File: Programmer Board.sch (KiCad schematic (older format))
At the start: 9 parts, among them J1 105-1103-001, J10 Conn_01x03, J11 105-1102-001, J12 105-1103-001, J2 Conn_01x03, J3 105-1102-001, J8 Conn_01x02, J9 Conn_02x18_Odd_Even

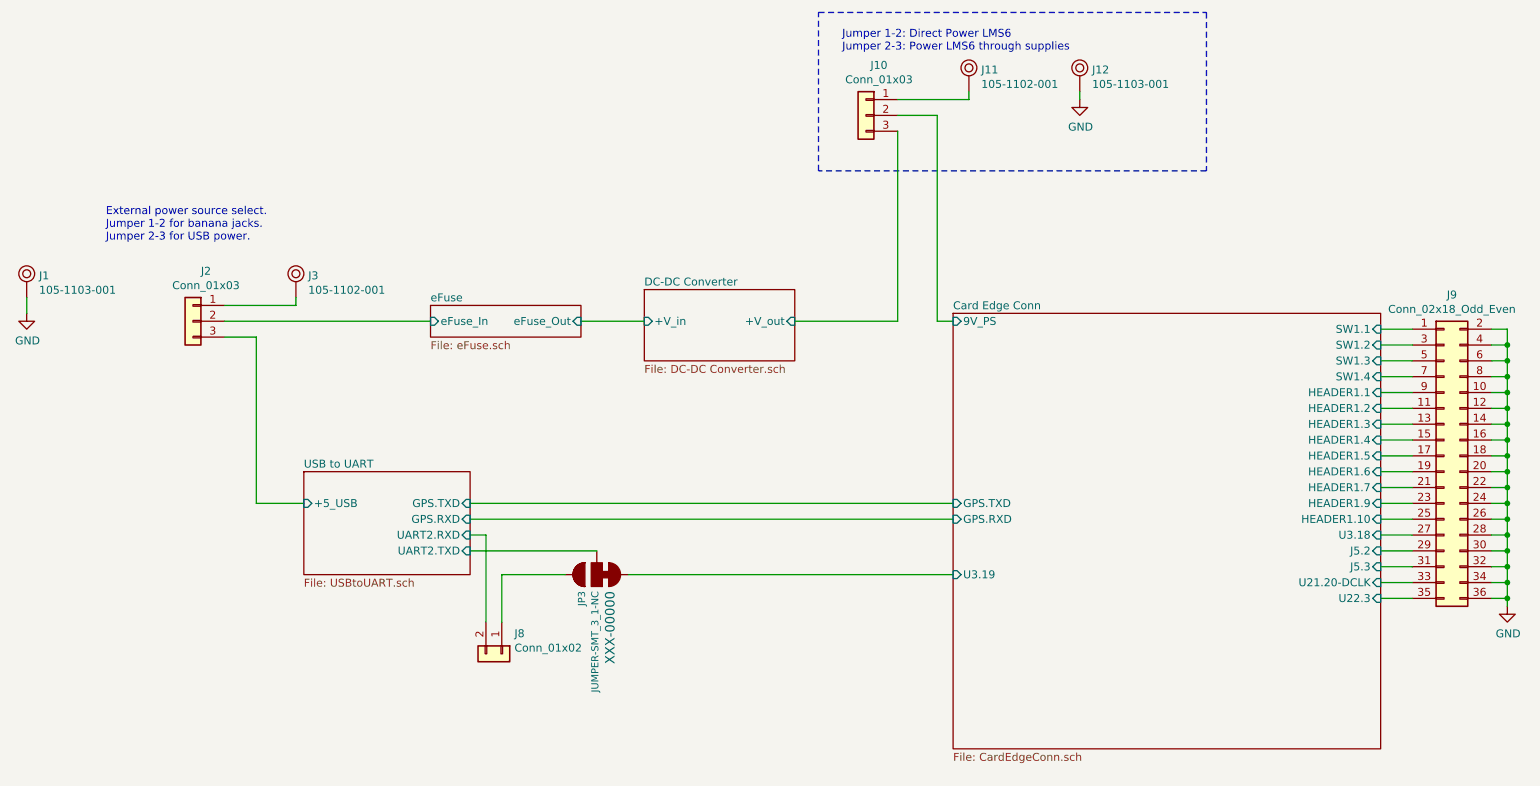
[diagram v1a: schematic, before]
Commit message: Changed J9 connections to help with layout.
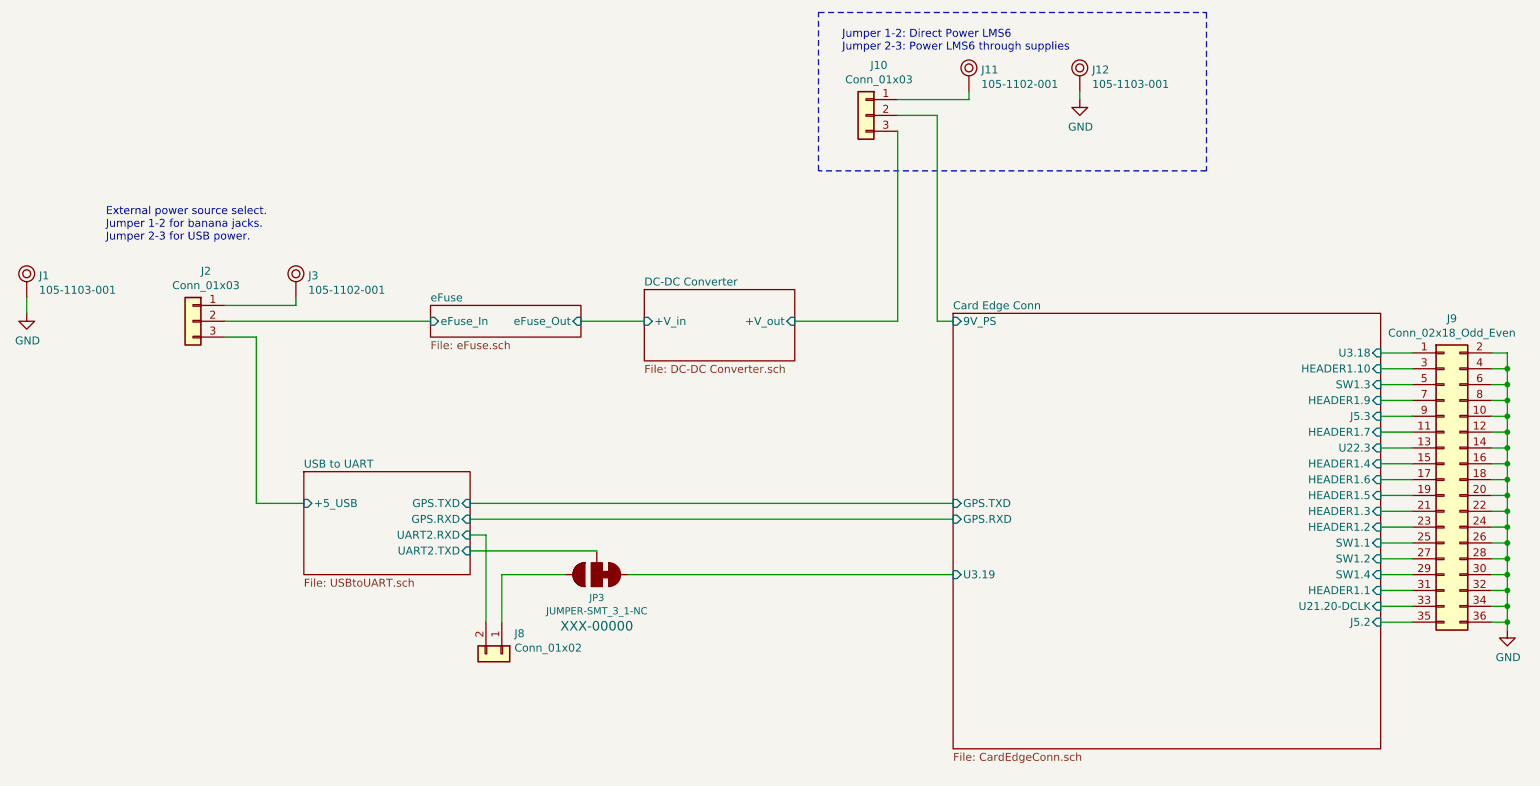
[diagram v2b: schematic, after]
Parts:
- JP3: footprint SMT-JUMPER_3_1-NC -> Jumpers:SMT-JUMPER_3_1-NC_TRACE_NO-SILK
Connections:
- net Card Edge Conn/HEADER1.1: now also J9.31 (Pin_31); no longer J9.9 (Pin_9)
- net Card Edge Conn/HEADER1.10: now also J9.3 (Pin_3); no longer J9.25 (Pin_25)
- net Card Edge Conn/HEADER1.2: now also J9.23 (Pin_23); no longer J9.11 (Pin_11)
- net Card Edge Conn/HEADER1.3: now also J9.21 (Pin_21); no longer J9.13 (Pin_13)
- net Card Edge Conn/HEADER1.5: now also J9.19 (Pin_19); no longer J9.17 (Pin_17)
- net Card Edge Conn/HEADER1.6: now also J9.17 (Pin_17); no longer J9.19 (Pin_19)
- net Card Edge Conn/HEADER1.7: now also J9.11 (Pin_11); no longer J9.21 (Pin_21)
- net Card Edge Conn/HEADER1.9: now also J9.7 (Pin_7); no longer J9.23 (Pin_23)
- net Card Edge Conn/J5.2: now also J9.35 (Pin_35); no longer J9.29 (Pin_29)
- net Card Edge Conn/J5.3: now also J9.9 (Pin_9); no longer J9.31 (Pin_31)
- net Card Edge Conn/SW1.1: now also J9.25 (Pin_25); no longer J9.1 (Pin_1)
- net Card Edge Conn/SW1.2: now also J9.27 (Pin_27); no longer J9.3 (Pin_3)
- net Card Edge Conn/SW1.4: now also J9.29 (Pin_29); no longer J9.7 (Pin_7)
- net Card Edge Conn/U22.3: now also J9.13 (Pin_13); no longer J9.35 (Pin_35)
- net Card Edge Conn/U3.18: now also J9.1 (Pin_1); no longer J9.27 (Pin_27)
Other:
- moved on the sheet: J9
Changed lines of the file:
@@
 Title "LMS6 Interface Board"
 Date "2020-10-17"
-Rev "5"
+Rev "6"
 Comp ""
-Comment1 "Rev 2: Added eFuse. Power Configurations."
-Comment2 "Rev 3: Changed sheet to US Letter"
-Comment3 "Rev 4: Fixed J9 hanging over border of sheet."
-Comment4 "Rev 5: Fixed J6 footprint and MPN info."
+Comment1 "Rev 3: Changed sheet to US Letter"
+Comment2 "Rev 4: Fixed J9 hanging over border of sheet."
+Comment3 "Rev 5: Fixed J6 footprint and MPN info."
+Comment4 "Rev 6: Fixed footprint issues. Changed J9 connections for layout."
 $EndDescr
 $Sheet
@@
 F0 "Card Edge Conn" 50
 F1 "CardEdgeConn.sch" 50
-F2 "U21.20-DCLK" I R 9450 4950 50
-F3 "SW1.1" I R 9450 3350 50
+F2 "U21.20-DCLK" I R 9450 5100 50
+F3 "SW1.1" I R 9450 4700 50
 F4 "GPS.TXD" I L 6750 4450 50
-F5 "U22.3" I R 9450 5050 50
-F6 "J5.3" I R 9450 4850 50
-F7 "SW1.3" I R 9450 3550 50
-F8 "U3.18" I R 9450 4650 50
+F5 "U22.3" I R 9450 4100 50
+F6 "J5.3" I R 9450 3900 50
+F7 "SW1.3" I R 9450 3700 50
+F8 "U3.18" I R 9450 3500 50
 F9 "GPS.RXD" I L 6750 4550 50
 F10 "U3.19" I L 6750 4900 50
-F11 "SW1.2" I R 9450 3450 50
-F12 "SW1.4" I R 9450 3650 50
-F13 "J5.2" I R 9450 4750 50
-F14 "HEADER1.1" I R 9450 3750 50
-F15 "HEADER1.2" I R 9450 3850 50
-F16 "HEADER1.3" I R 9450 3950 50
-F17 "HEADER1.4" I R 9450 4050 50
-F18 "HEADER1.5" I R 9450 4150 50
-F19 "HEADER1.6" I R 9450 4250 50
-F20 "HEADER1.7" I R 9450 4350 50
-F21 "HEADER1.9" I R 9450 4450 50
-F22 "HEADER1.10" I R 9450 4550 50
+F11 "SW1.2" I R 9450 4800 50
+F12 "SW1.4" I R 9450 4900 50
+F13 "J5.2" I R 9450 5200 50
+F14 "HEADER1.1" I R 9450 5000 50
+F15 "HEADER1.2" I R 9450 4600 50
+F16 "HEADER1.3" I R 9450 4500 50
+F17 "HEADER1.4" I R 9450 4200 50
+F18 "HEADER1.5" I R 9450 4400 50
+F19 "HEADER1.6" I R 9450 4300 50
+F20 "HEADER1.7" I R 9450 4000 50
+F21 "HEADER1.9" I R 9450 3800 50
+F22 "HEADER1.10" I R 9450 3600 50
 F23 "9V_PS" I L 6750 3300 50
 $EndSheet
@@
 AR Path="/5F7C6408/5F8F06E0" Ref="JP?"  Part="1"
 AR Path="/5F8F06E0" Ref="JP3"  Part="1"
-F 0 "JP3" H 4604 4995 45  0000 L CNN
-F 1 "JUMPER-SMT_3_1-NC" H 4604 4911 45  0000 L CNN
-F 2 "SMT-JUMPER_3_1-NC" H 4500 5150 20  0001 C CNN
+F 0 "JP3" V 4646 4900 45  0000 C CNN
+F 1 "JUMPER-SMT_3_1-NC" V 4730 4900 45  0000 C CNN
+F 2 "Jumpers:SMT-JUMPER_3_1-NC_TRACE_NO-SILK" H 4500 5150 20  0001 C CNN
 F 3 "" V 4500 4845 60  0001 C CNN
-F 4 "XXX-00000" H 4604 4816 60  0000 L CNN "PROD_ID"
+F 4 "XXX-00000" V 4825 4900 60  0000 C CNN "PROD_ID"
 	1    4500 4900
 	0    -1   1    0
@@
 L Connector_Generic:Conn_02x18_Odd_Even J9
 U 1 1 5F8F3B51
-P 9850 4150
-F 0 "J9" H 9900 5167 50  0000 C CNN
-F 1 "Conn_02x18_Odd_Even" H 9900 5076 50  0000 C CNN
-F 2 "Connector_PinHeader_2.54mm:PinHeader_2x18_P2.54mm_Vertical" H 9850 4150 50  0001 C CNN
-F 3 "https://drawings-pdf.s3.amazonaws.com/11636.pdf" H 9850 4150 50  0001 C CNN
-F 4 "Sullins Connector Solutions" H 9850 4150 50  0001 C CNN "Manufacturer"
-F 5 "PREC020DAAN-RC" H 9850 4150 50  0001 C CNN "MPN"
-	1    9850 4150
-	1    0    0    -1
-$EndComp
-Wire Wire Line
-	9650 3350 9450 3350
-Wire Wire Line
-	9450 3450 9650 3450
-Wire Wire Line
-	9650 3550 9450 3550
-Wire Wire Line
-	9450 3650 9650 3650
-Wire Wire Line
-	9650 3750 9450 3750
-Wire Wire Line
-	9450 3850 9650 3850
-Wire Wire Line
-	9650 3950 9450 3950
-Wire Wire Line
-	9450 4050 9650 4050
-Wire Wire Line
-	9650 4150 9450 4150
-Wire Wire Line
-	9450 4250 9650 4250
-Wire Wire Line
-	9650 4350 9450 4350
-Wire Wire Line
-	9450 4450 9650 4450
-Wire Wire Line
-	9650 4550 9450 4550
-Wire Wire Line
-	9450 4650 9650 4650
-Wire Wire Line
-	9650 4750 9450 4750
-Wire Wire Line
-	9450 4850 9650 4850
-Wire Wire Line
-	9650 4950 9450 4950
-Wire Wire Line
-	9450 5050 9650 5050
+P 9850 4300
+F 0 "J9" H 9900 5317 50  0000 C CNN
+F 1 "Conn_02x18_Odd_Even" H 9900 5226 50  0000 C CNN
+F 2 "Connector_PinHeader_2.54mm:PinHeader_2x18_P2.54mm_Vertical" H 9850 4300 50  0001 C CNN
+F 3 "https://drawings-pdf.s3.amazonaws.com/11636.pdf" H 9850 4300 50  0001 C CNN
+F 4 "Sullins Connector Solutions" H 9850 4300 50  0001 C CNN "Manufacturer"
+F 5 "PREC020DAAN-RC" H 9850 4300 50  0001 C CNN "MPN"
+	1    9850 4300
+	1    0    0    -1
+$EndComp
 $Comp
 L power:GND #PWR018
 U 1 1 5F8FB83E
-P 10250 5100
-F 0 "#PWR018" H 10250 4850 50  0001 C CNN
-F 1 "GND" H 10255 4927 50  0000 C CNN
-F 2 "" H 10250 5100 50  0001 C CNN
-F 3 "" H 10250 5100 50  0001 C CNN
-	1    10250 5100
-	1    0    0    -1
-$EndComp
-Wire Wire Line
-	10250 5100 10250 5050
-Wire Wire Line
-	10250 5050 10150 5050
-Wire Wire Line
-	10150 3350 10250 3350
-Connection ~ 10250 5050
-Wire Wire Line
-	10150 4950 10250 4950
-Connection ~ 10250 4950
-Wire Wire Line
-	10250 4950 10250 5050
-Wire Wire Line
-	10150 4850 10250 4850
-Connection ~ 10250 4850
-Wire Wire Line
-	10250 4850 10250 4950
-Wire Wire Line
-	10150 4750 10250 4750
-Connection ~ 10250 4750
-Wire Wire Line
-	10250 4750 10250 4850
-Wire Wire Line
-	10150 4650 10250 4650
-Connection ~ 10250 4650
-Wire Wire Line
-	10250 4650 10250 4750
-Wire Wire Line
-	10150 4550 10250 4550
-Connection ~ 10250 4550
-Wire Wire Line
-	10250 4550 10250 4650
-Wire Wire Line
-	10150 4450 10250 4450
-Connection ~ 10250 4450
-Wire Wire Line
-	10250 4450 10250 4550
-Wire Wire Line
-	10150 4350 10250 4350
-Connection ~ 10250 4350
-Wire Wire Line
-	10250 4350 10250 4450
-Wire Wire Line
-	10150 4250 10250 4250
-Wire Wire Line
-	10250 3350 10250 3450
-Connection ~ 10250 4250
-Wire Wire Line
-	10250 4250 10250 4350
-Wire Wire Line
-	10150 4150 10250 4150
-Connection ~ 10250 4150
-Wire Wire Line
-	10250 4150 10250 4250
-Wire Wire Line
-	10150 4050 10250 4050
-Connection ~ 10250 4050
-Wire Wire Line
-	10250 4050 10250 4150
-Wire Wire Line
-	10150 3950 10250 3950
-Connection ~ 10250 3950
-Wire Wire Line
-	10250 3950 10250 4050
-Wire Wire Line
-	10150 3850 10250 3850
-Connection ~ 10250 3850
-Wire Wire Line
-	10250 3850 10250 3950
-Wire Wire Line
-	10150 3750 10250 3750
-Connection ~ 10250 3750
-Wire Wire Line
-	10250 3750 10250 3850
-Wire Wire Line
-	10150 3650 10250 3650
-Connection ~ 10250 3650
-Wire Wire Line
-	10250 3650 10250 3750
-Wire Wire Line
-	10150 3550 10250 3550
-Connection ~ 10250 3550
-Wire Wire Line
-	10250 3550 10250 3650
-Wire Wire Line
-	10150 3450 10250 3450
-Connection ~ 10250 3450
-Wire Wire Line
-	10250 3450 10250 3550
+P 10250 5250
+F 0 "#PWR018" H 10250 5000 50  0001 C CNN
+F 1 "GND" H 10255 5077 50  0000 C CNN
+F 2 "" H 10250 5250 50  0001 C CNN
+F 3 "" H 10250 5250 50  0001 C CNN
+	1    10250 5250
+	1    0    0    -1
+$EndComp
+Wire Wire Line
+	10250 5250 10250 5200
+Wire Wire Line
+	10250 5200 10150 5200
+Wire Wire Line
+	10150 3500 10250 3500
+Connection ~ 10250 5200
+Wire Wire Line
+	10150 5100 10250 5100
+Connection ~ 10250 5100
+Wire Wire Line
+	10250 5100 10250 5200
+Wire Wire Line
+	10150 5000 10250 5000
+Connection ~ 10250 5000
+Wire Wire Line
+	10250 5000 10250 5100
+Wire Wire Line
+	10150 4900 10250 4900
+Connection ~ 10250 4900
+Wire Wire Line
+	10250 4900 10250 5000
+Wire Wire Line
+	10150 4800 10250 4800
+Connection ~ 10250 4800
+Wire Wire Line
+	10250 4800 10250 4900
+Wire Wire Line
+	10150 4700 10250 4700
+Connection ~ 10250 4700
+Wire Wire Line
+	10250 4700 10250 4800
+Wire Wire Line
+	10150 4600 10250 4600
+Connection ~ 10250 4600
+Wire Wire Line
+	10250 4600 10250 4700
+Wire Wire Line
+	10150 4500 10250 4500
+Connection ~ 10250 4500
+Wire Wire Line
+	10250 4500 10250 4600
+Wire Wire Line
+	10150 4400 10250 4400
+Wire Wire Line
+	10250 3500 10250 3600
+Connection ~ 10250 4400
+Wire Wire Line
+	10250 4400 10250 4500
+Wire Wire Line
+	10150 4300 10250 4300
+Connection ~ 10250 4300
+Wire Wire Line
+	10250 4300 10250 4400
+Wire Wire Line
+	10150 4200 10250 4200
+Connection ~ 10250 4200
+Wire Wire Line
+	10250 4200 10250 4300
+Wire Wire Line
+	10150 4100 10250 4100
+Connection ~ 10250 4100
+Wire Wire Line
+	10250 4100 10250 4200
+Wire Wire Line
+	10150 4000 10250 4000
+Connection ~ 10250 4000
+Wire Wire Line
+	10250 4000 10250 4100
+Wire Wire Line
+	10150 3900 10250 3900
+Connection ~ 10250 3900
+Wire Wire Line
+	10250 3900 10250 4000
+Wire Wire Line
+	10150 3800 10250 3800
+Connection ~ 10250 3800
+Wire Wire Line
+	10250 3800 10250 3900
+Wire Wire Line
+	10150 3700 10250 3700
+Connection ~ 10250 3700
+Wire Wire Line
+	10250 3700 10250 3800
+Wire Wire Line
+	10150 3600 10250 3600
+Connection ~ 10250 3600
+Wire Wire Line
+	10250 3600 10250 3700
 $Sheet
 S 3450 3200 950  200
@@
 Wire Notes Line
 	5900 2350 5900 1350
+Wire Wire Line
+	9450 3500 9650 3500
+Wire Wire Line
+	9450 3600 9650 3600
+Wire Wire Line
+	9450 3700 9650 3700
+Wire Wire Line
+	9450 3800 9650 3800
+Wire Wire Line
+	9450 3900 9650 3900
+Wire Wire Line
+	9450 4000 9650 4000
+Wire Wire Line
+	9450 4100 9650 4100
+Wire Wire Line
+	9450 4200 9650 4200
+Wire Wire Line
+	9450 4300 9650 4300
+Wire Wire Line
+	9450 4400 9650 4400
+Wire Wire Line
+	9450 4500 9650 4500
+Wire Wire Line
+	9450 4600 9650 4600
+Wire Wire Line
+	9450 4700 9650 4700
+Wire Wire Line
+	9450 4800 9650 4800
+Wire Wire Line
+	9450 4900 9650 4900
+Wire Wire Line
+	9450 5000 9650 5000
+Wire Wire Line
+	9450 5100 9650 5100
+Wire Wire Line
+	9450 5200 9650 5200
 $EndSCHEMATC

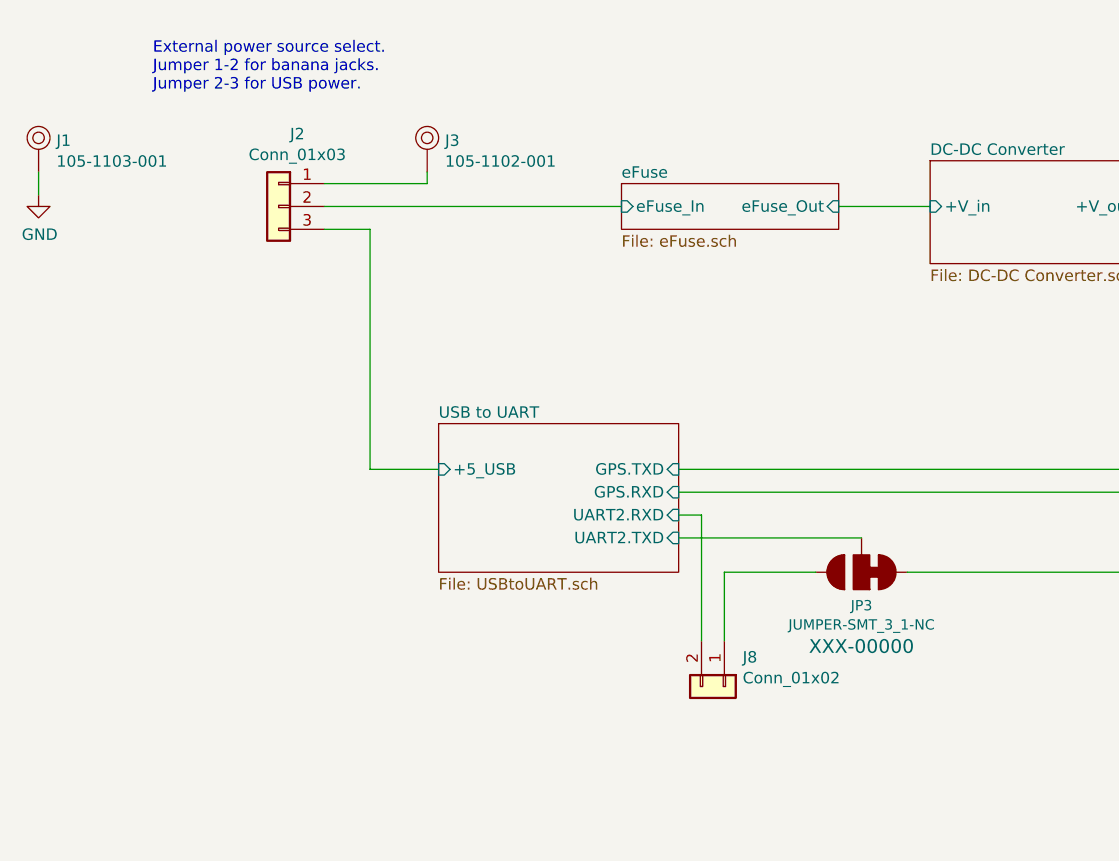
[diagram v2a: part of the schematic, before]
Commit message: Changed crystal for resonator. Board Layout.
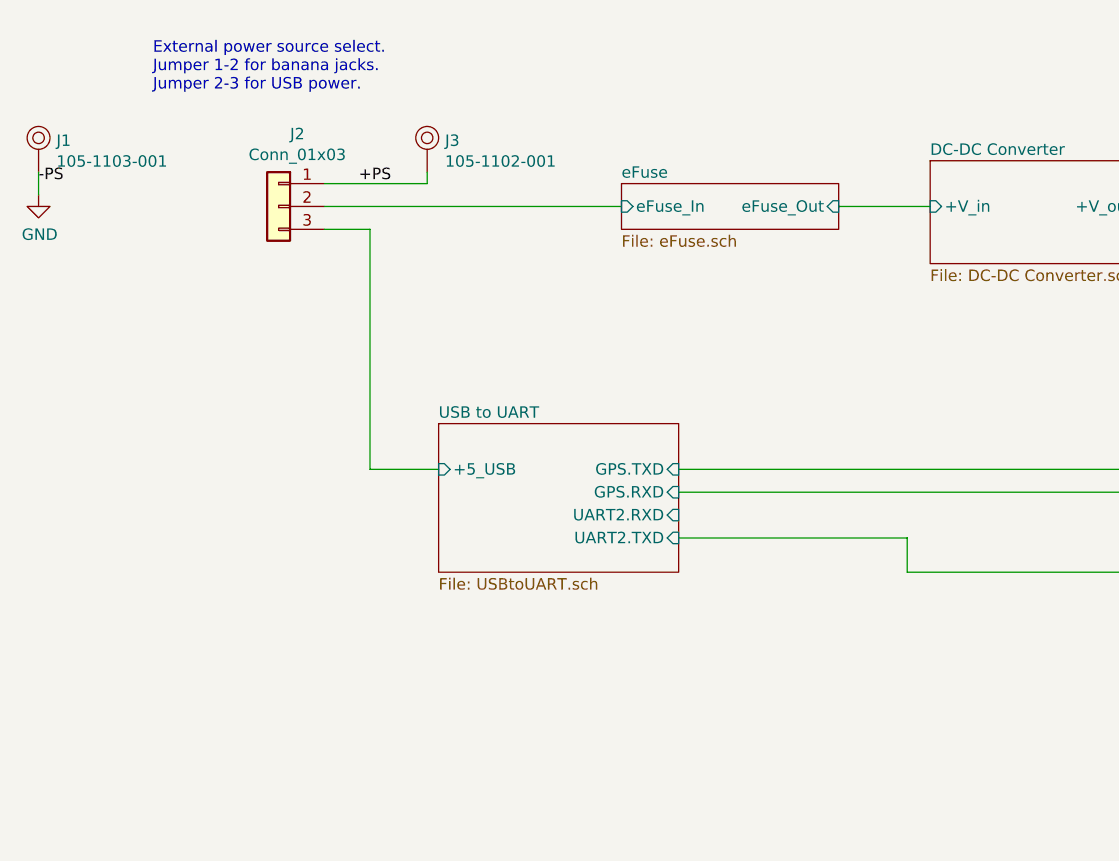
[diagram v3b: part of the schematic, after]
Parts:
- removed J8: Conn_01x02, Connector_PinHeader_2.54mm:PinHeader_1x02_P2.54mm_Vertical, symbol Connector_Generic:Conn_01x02
- removed JP3: JUMPER-SMT_3_1-NC, Jumpers:SMT-JUMPER_3_1-NC_TRACE_NO-SILK, symbol SparkFun-Jumpers:JUMPER-SMT_3_1-NC
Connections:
- net +PS: now reaches J2.1 (Pin_1), J3.1
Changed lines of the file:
@@
 Comment2 "Rev 4: Fixed J9 hanging over border of sheet."
 Comment3 "Rev 5: Fixed J6 footprint and MPN info."
-Comment4 "Rev 6: Fixed footprint issues. Changed J9 connections for layout."
+Comment4 "Rev 6: Fixed footprint issues. Changed J9 connections for layout. Changed Y1."
 $EndDescr
 $Sheet
@@
 Wire Wire Line
 	3700 4550 6750 4550
-$Comp
-L SparkFun-Jumpers:JUMPER-SMT_3_1-NC JP?
-U 1 1 5F8F06E0
-P 4500 4900
-AR Path="/5F7C6408/5F8F06E0" Ref="JP?"  Part="1"
-AR Path="/5F8F06E0" Ref="JP3"  Part="1"
-F 0 "JP3" V 4646 4900 45  0000 C CNN
-F 1 "JUMPER-SMT_3_1-NC" V 4730 4900 45  0000 C CNN
-F 2 "Jumpers:SMT-JUMPER_3_1-NC_TRACE_NO-SILK" H 4500 5150 20  0001 C CNN
-F 3 "" V 4500 4845 60  0001 C CNN
-F 4 "XXX-00000" V 4825 4900 60  0000 C CNN "PROD_ID"
-	1    4500 4900
-	0    -1   1    0
-$EndComp
-Wire Wire Line
-	3700 4750 4500 4750
 Wire Wire Line
 	4700 4900 6750 4900
-$Comp
-L Connector_Generic:Conn_01x02 J8
-U 1 1 5F8F12C1
-P 3900 5400
-F 0 "J8" V 3772 5480 50  0000 L CNN
-F 1 "Conn_01x02" V 3863 5480 50  0000 L CNN
-F 2 "Connector_PinHeader_2.54mm:PinHeader_1x02_P2.54mm_Vertical" H 3900 5400 50  0001 C CNN
-F 3 "~" H 3900 5400 50  0001 C CNN
-F 4 "Würth Elektronik" V 3900 5400 50  0001 C CNN "Manufacturer"
-F 5 "61300211121" V 3900 5400 50  0001 C CNN "MPN"
-	1    3900 5400
-	0    1    1    0
-$EndComp
-Wire Wire Line
-	3900 5200 3900 4900
-Wire Wire Line
-	3900 4900 4300 4900
-Wire Wire Line
-	3800 5200 3800 4650
-Wire Wire Line
-	3800 4650 3700 4650
 $Comp
 L Connector_Generic:Conn_02x18_Odd_Even J9
@@
 Wire Wire Line
 	9450 5200 9650 5200
+Wire Wire Line
+	4700 4750 4700 4900
+Wire Wire Line
+	3700 4750 4700 4750
+Text Label 2300 3200 0    50   ~ 0
++PS
+Text Label 900  3200 0    50   ~ 0
+-PS
 $EndSCHEMATC
